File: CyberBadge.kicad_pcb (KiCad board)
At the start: 2 copper layers, 87.5 x 41 mm, 382 parts, among them J1 USB_C_Receptacle_USB2.0, J2 BAT_CONN, Q1 MMBT3904, Q2 MMBT3904, SW1 B_RST, SW2 B1/BOOT, U1 USBLC6-2SC6, U2 CP2102N-A01-GQFN28, U3 ESP32-WROOM-32, U4 SPX3819M5-L-3-3, U5 BQ24073RGT

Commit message: i forgor
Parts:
- removed REF**: SW_SPDT_PCM12, Button_Switch_SMD:SW_SPDT_PCM12
- added C180: 100n, Capacitor_SMD:C_0201_0603Metric, F.Cu at (143.5, 119.5)
- added Q3: FS8205A, Package_SO:TSSOP-8_4.4x3mm_P0.65mm, F.Cu at (151.2, 111.2)
- added R19: 200, Resistor_SMD:R_0201_0603Metric, F.Cu at (145.9, 119.5)
- added R20: 1k, Resistor_SMD:R_0201_0603Metric, F.Cu at (148.4, 119.5)
- added R21: 10k, Resistor_SMD:R_0201_0603Metric, F.Cu at (152.2, 119.4)
- added U6: DW01x, Package_TO_SOT_SMD:SOT-23-6, F.Cu at (153.6, 116.3)
- moved C10 0.80 mm to (149.9, 99.0)
- moved C7 0.80 mm to (146.4, 102.5)
- moved C8 0.80 mm to (143.9, 100.5)
- moved R16 0.80 mm to (144.9, 100.5)
- moved R17 0.80 mm to (148.4, 102.5)
- moved R18 0.80 mm to (149.9, 100.0)
- moved U5 0.80 mm to (147.4, 100.0)
- moved U1 0.32 mm to (152.3, 105.1)

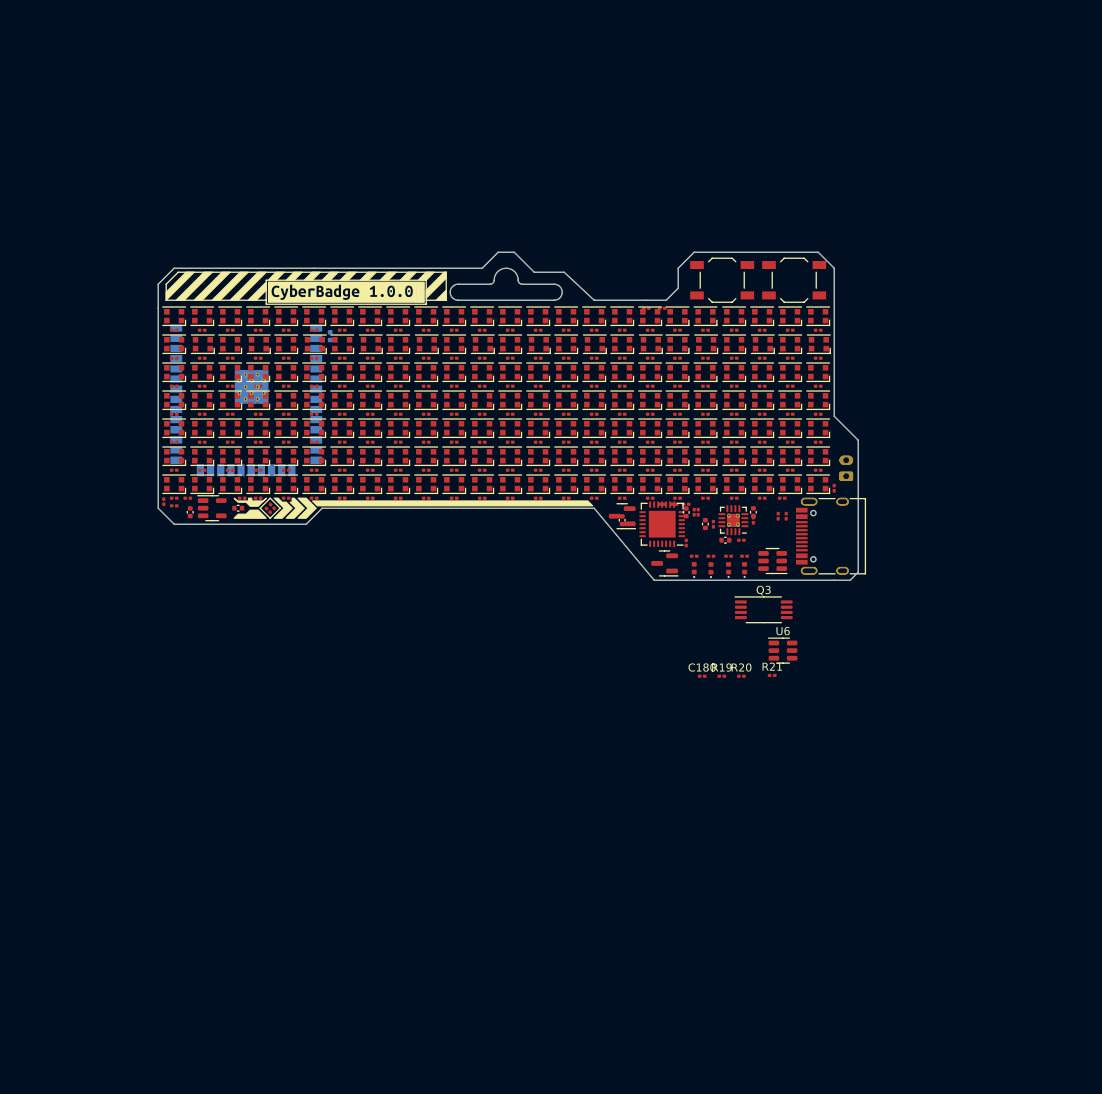
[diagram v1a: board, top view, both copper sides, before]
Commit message: change pixel count
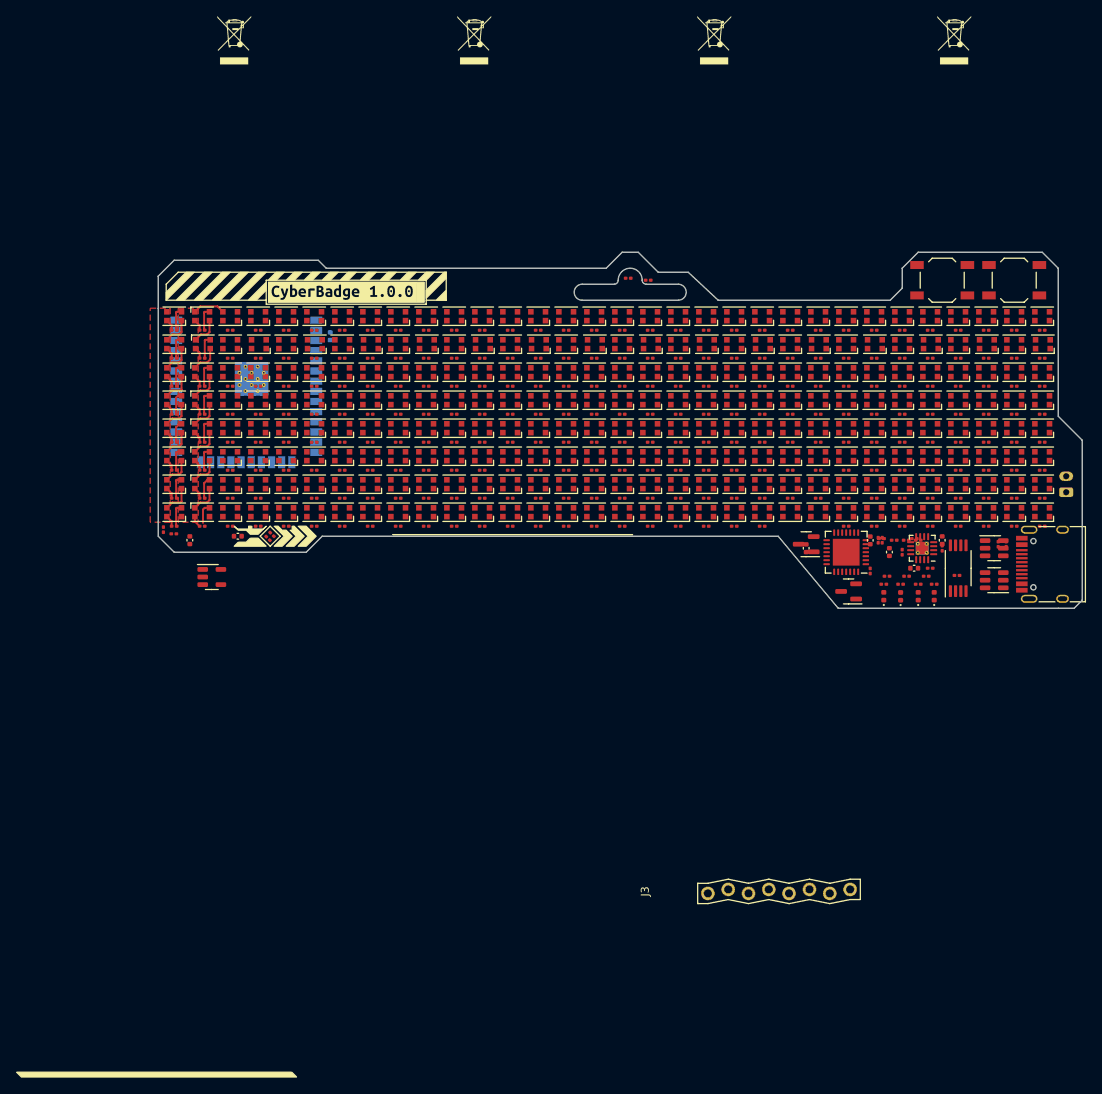
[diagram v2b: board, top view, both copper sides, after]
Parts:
- added C181: 100n, Capacitor_SMD:C_0201_0603Metric, F.Cu at (77.5, 97.2)
- added C182: 100n, Capacitor_SMD:C_0201_0603Metric, F.Cu at (81.0, 97.2)
- added C183: 100n, Capacitor_SMD:C_0201_0603Metric, F.Cu at (84.5, 97.2)
- added C184: 100n, Capacitor_SMD:C_0201_0603Metric, F.Cu at (88.0, 97.2)
- added C185: 100n, Capacitor_SMD:C_0201_0603Metric, F.Cu at (91.5, 97.2)
- added C186: 100n, Capacitor_SMD:C_0201_0603Metric, F.Cu at (95.0, 97.2)
- added C187: 100n, Capacitor_SMD:C_0201_0603Metric, F.Cu at (98.5, 97.2)
- added C188: 100n, Capacitor_SMD:C_0201_0603Metric, F.Cu at (102.0, 97.2)
- added C189: 100n, Capacitor_SMD:C_0201_0603Metric, F.Cu at (105.5, 97.2)
- added C190: 100n, Capacitor_SMD:C_0201_0603Metric, F.Cu at (109.0, 97.2)
- added C191: 100n, Capacitor_SMD:C_0201_0603Metric, F.Cu at (112.5, 97.2)
- added C192: 100n, Capacitor_SMD:C_0201_0603Metric, F.Cu at (116.0, 97.2)
- added C193: 100n, Capacitor_SMD:C_0201_0603Metric, F.Cu at (119.5, 97.2)
- added C194: 100n, Capacitor_SMD:C_0201_0603Metric, F.Cu at (123.0, 97.2)
- added C195: 100n, Capacitor_SMD:C_0201_0603Metric, F.Cu at (126.5, 97.2)
- added C196: 100n, Capacitor_SMD:C_0201_0603Metric, F.Cu at (130.0, 97.2)
- added C197: 100n, Capacitor_SMD:C_0201_0603Metric, F.Cu at (133.5, 97.2)
- added C198: 100n, Capacitor_SMD:C_0201_0603Metric, F.Cu at (137.0, 97.2)
- added C199: 100n, Capacitor_SMD:C_0201_0603Metric, F.Cu at (140.5, 97.2)
- added C200: 100n, Capacitor_SMD:C_0201_0603Metric, F.Cu at (144.0, 97.2)
- added C201: 100n, Capacitor_SMD:C_0201_0603Metric, F.Cu at (147.5, 97.2)
- added C202: 100n, Capacitor_SMD:C_0201_0603Metric, F.Cu at (151.0, 97.2)
- added C203: 100n, Capacitor_SMD:C_0201_0603Metric, F.Cu at (154.5, 97.2)
- added C204: 100n, Capacitor_SMD:C_0201_0603Metric, F.Cu at (158.0, 97.2)
- added C205: 100n, Capacitor_SMD:C_0201_0603Metric, F.Cu at (161.5, 76.2)
- added C206: 100n, Capacitor_SMD:C_0201_0603Metric, F.Cu at (165.0, 76.2)
- added C207: 100n, Capacitor_SMD:C_0201_0603Metric, F.Cu at (161.5, 79.8)
- added C208: 100n, Capacitor_SMD:C_0201_0603Metric, F.Cu at (165.0, 79.8)
- added C209: 100n, Capacitor_SMD:C_0201_0603Metric, F.Cu at (161.5, 83.2)
- added C210: 100n, Capacitor_SMD:C_0201_0603Metric, F.Cu at (165.0, 83.2)
- added C211: 100n, Capacitor_SMD:C_0201_0603Metric, F.Cu at (161.5, 86.8)
- added C212: 100n, Capacitor_SMD:C_0201_0603Metric, F.Cu at (165.0, 86.8)
- added C213: 100n, Capacitor_SMD:C_0201_0603Metric, F.Cu at (161.5, 90.2)
- added C214: 100n, Capacitor_SMD:C_0201_0603Metric, F.Cu at (165.0, 90.2)
- added C215: 100n, Capacitor_SMD:C_0201_0603Metric, F.Cu at (161.5, 93.8)
- added C216: 100n, Capacitor_SMD:C_0201_0603Metric, F.Cu at (165.0, 93.8)
- added C217: 100n, Capacitor_SMD:C_0201_0603Metric, F.Cu at (161.5, 97.2)
- added C218: 100n, Capacitor_SMD:C_0201_0603Metric, F.Cu at (165.0, 97.2)
- added C219: 100n, Capacitor_SMD:C_0201_0603Metric, F.Cu at (161.5, 100.8)
- added C220: 100n, Capacitor_SMD:C_0201_0603Metric, F.Cu at (165.0, 100.8)
- added C221: 100n, Capacitor_SMD:C_0201_0603Metric, F.Cu at (168.5, 76.2)
- added C222: 100n, Capacitor_SMD:C_0201_0603Metric, F.Cu at (172.0, 76.2)
- added C223: 100n, Capacitor_SMD:C_0201_0603Metric, F.Cu at (168.5, 79.8)
- added C224: 100n, Capacitor_SMD:C_0201_0603Metric, F.Cu at (172.0, 79.8)
- added C225: 100n, Capacitor_SMD:C_0201_0603Metric, F.Cu at (168.5, 83.2)
- added C226: 100n, Capacitor_SMD:C_0201_0603Metric, F.Cu at (172.0, 83.2)
- added C227: 100n, Capacitor_SMD:C_0201_0603Metric, F.Cu at (168.5, 86.8)
- added C228: 100n, Capacitor_SMD:C_0201_0603Metric, F.Cu at (172.0, 86.8)
- added C229: 100n, Capacitor_SMD:C_0201_0603Metric, F.Cu at (168.5, 90.2)
- added C230: 100n, Capacitor_SMD:C_0201_0603Metric, F.Cu at (172.0, 90.2)
- added C231: 100n, Capacitor_SMD:C_0201_0603Metric, F.Cu at (168.5, 93.8)
- added C232: 100n, Capacitor_SMD:C_0201_0603Metric, F.Cu at (172.0, 93.8)
- added C233: 100n, Capacitor_SMD:C_0201_0603Metric, F.Cu at (168.5, 97.2)
- added C234: 100n, Capacitor_SMD:C_0201_0603Metric, F.Cu at (172.0, 97.2)
- added C235: 100n, Capacitor_SMD:C_0201_0603Metric, F.Cu at (168.5, 100.8)
- added C236: 100n, Capacitor_SMD:C_0201_0603Metric, F.Cu at (172.0, 100.8)
- added C237: 100n, Capacitor_SMD:C_0201_0603Metric, F.Cu at (175.5, 76.2)
- added C238: 100n, Capacitor_SMD:C_0201_0603Metric, F.Cu at (179.0, 76.2)
- added C239: 100n, Capacitor_SMD:C_0201_0603Metric, F.Cu at (175.5, 79.8)
- added C240: 100n, Capacitor_SMD:C_0201_0603Metric, F.Cu at (179.0, 79.8)
- added C241: 100n, Capacitor_SMD:C_0201_0603Metric, F.Cu at (175.5, 83.2)
- added C242: 100n, Capacitor_SMD:C_0201_0603Metric, F.Cu at (179.0, 83.2)
- added C243: 100n, Capacitor_SMD:C_0201_0603Metric, F.Cu at (175.5, 86.8)
- added C244: 100n, Capacitor_SMD:C_0201_0603Metric, F.Cu at (179.0, 86.8)
- added C245: 100n, Capacitor_SMD:C_0201_0603Metric, F.Cu at (175.5, 90.2)
- added C246: 100n, Capacitor_SMD:C_0201_0603Metric, F.Cu at (179.0, 90.2)
- added C247: 100n, Capacitor_SMD:C_0201_0603Metric, F.Cu at (175.5, 93.8)
- added C248: 100n, Capacitor_SMD:C_0201_0603Metric, F.Cu at (179.0, 93.8)
- added C249: 100n, Capacitor_SMD:C_0201_0603Metric, F.Cu at (175.5, 97.2)
- added C250: 100n, Capacitor_SMD:C_0201_0603Metric, F.Cu at (179.0, 97.2)
- added C251: 100n, Capacitor_SMD:C_0201_0603Metric, F.Cu at (175.5, 100.8)
- added C252: 100n, Capacitor_SMD:C_0201_0603Metric, F.Cu at (179.0, 100.8)
- added C253: 100n, Capacitor_SMD:C_0201_0603Metric, F.Cu at (182.5, 76.2)
- added C254: 100n, Capacitor_SMD:C_0201_0603Metric, F.Cu at (186.0, 76.2)
- added C255: 100n, Capacitor_SMD:C_0201_0603Metric, F.Cu at (182.5, 79.8)
- added C256: 100n, Capacitor_SMD:C_0201_0603Metric, F.Cu at (186.0, 79.8)
- added C257: 100n, Capacitor_SMD:C_0201_0603Metric, F.Cu at (182.5, 83.2)
- added C258: 100n, Capacitor_SMD:C_0201_0603Metric, F.Cu at (186.0, 83.2)
- added C259: 100n, Capacitor_SMD:C_0201_0603Metric, F.Cu at (182.5, 86.8)
- added C260: 100n, Capacitor_SMD:C_0201_0603Metric, F.Cu at (186.0, 86.8)
- added C261: 100n, Capacitor_SMD:C_0201_0603Metric, F.Cu at (182.5, 90.2)
- added C262: 100n, Capacitor_SMD:C_0201_0603Metric, F.Cu at (186.0, 90.2)
- added C263: 100n, Capacitor_SMD:C_0201_0603Metric, F.Cu at (182.5, 93.8)
- added C264: 100n, Capacitor_SMD:C_0201_0603Metric, F.Cu at (186.0, 93.8)
- added C265: 100n, Capacitor_SMD:C_0201_0603Metric, F.Cu at (182.5, 97.2)
- added C266: 100n, Capacitor_SMD:C_0201_0603Metric, F.Cu at (186.0, 97.2)
- added C267: 100n, Capacitor_SMD:C_0201_0603Metric, F.Cu at (182.5, 100.8)
- added C268: 100n, Capacitor_SMD:C_0201_0603Metric, F.Cu at (186.0, 100.8)
- added D173: WS2812B, Critbit_lib:LED_WS2812B-2020_pinsRenumbered, F.Cu at (77.5, 95.5)
- added D174: WS2812B, Critbit_lib:LED_WS2812B-2020_pinsRenumbered, F.Cu at (81.0, 95.5)
- added D175: WS2812B, Critbit_lib:LED_WS2812B-2020_pinsRenumbered, F.Cu at (84.5, 95.5)
- added D176: WS2812B, Critbit_lib:LED_WS2812B-2020_pinsRenumbered, F.Cu at (88.0, 95.5)
- added D177: WS2812B, Critbit_lib:LED_WS2812B-2020_pinsRenumbered, F.Cu at (91.5, 95.5)
- added D178: WS2812B, Critbit_lib:LED_WS2812B-2020_pinsRenumbered, F.Cu at (95.0, 95.5)
- added D179: WS2812B, Critbit_lib:LED_WS2812B-2020_pinsRenumbered, F.Cu at (98.5, 95.5)
- added D180: WS2812B, Critbit_lib:LED_WS2812B-2020_pinsRenumbered, F.Cu at (102.0, 95.5)
- added D181: WS2812B, Critbit_lib:LED_WS2812B-2020_pinsRenumbered, F.Cu at (105.5, 95.5)
- added D182: WS2812B, Critbit_lib:LED_WS2812B-2020_pinsRenumbered, F.Cu at (109.0, 95.5)
- added D183: WS2812B, Critbit_lib:LED_WS2812B-2020_pinsRenumbered, F.Cu at (112.5, 95.5)
- added D184: WS2812B, Critbit_lib:LED_WS2812B-2020_pinsRenumbered, F.Cu at (116.0, 95.5)
- added D185: WS2812B, Critbit_lib:LED_WS2812B-2020_pinsRenumbered, F.Cu at (119.5, 95.5)
- added D186: WS2812B, Critbit_lib:LED_WS2812B-2020_pinsRenumbered, F.Cu at (123.0, 95.5)
- added D187: WS2812B, Critbit_lib:LED_WS2812B-2020_pinsRenumbered, F.Cu at (126.5, 95.5)
- added D188: WS2812B, Critbit_lib:LED_WS2812B-2020_pinsRenumbered, F.Cu at (130.0, 95.5)
- added D189: WS2812B, Critbit_lib:LED_WS2812B-2020_pinsRenumbered, F.Cu at (133.5, 95.5)
- added D190: WS2812B, Critbit_lib:LED_WS2812B-2020_pinsRenumbered, F.Cu at (137.0, 95.5)
- added D191: WS2812B, Critbit_lib:LED_WS2812B-2020_pinsRenumbered, F.Cu at (140.5, 95.5)
- added D192: WS2812B, Critbit_lib:LED_WS2812B-2020_pinsRenumbered, F.Cu at (144.0, 95.5)
- added D193: WS2812B, Critbit_lib:LED_WS2812B-2020_pinsRenumbered, F.Cu at (147.5, 95.5)
- added D194: WS2812B, Critbit_lib:LED_WS2812B-2020_pinsRenumbered, F.Cu at (151.0, 95.5)
- added D195: WS2812B, Critbit_lib:LED_WS2812B-2020_pinsRenumbered, F.Cu at (154.5, 95.5)
- added D196: WS2812B, Critbit_lib:LED_WS2812B-2020_pinsRenumbered, F.Cu at (158.0, 95.5)
- added D197: WS2812B, Critbit_lib:LED_WS2812B-2020_pinsRenumbered, F.Cu at (161.5, 74.5)
- added D198: WS2812B, Critbit_lib:LED_WS2812B-2020_pinsRenumbered, F.Cu at (165.0, 74.5)
- added D199: WS2812B, Critbit_lib:LED_WS2812B-2020_pinsRenumbered, F.Cu at (161.5, 78.0)
- added D200: WS2812B, Critbit_lib:LED_WS2812B-2020_pinsRenumbered, F.Cu at (165.1, 78.0)
- added D201: WS2812B, Critbit_lib:LED_WS2812B-2020_pinsRenumbered, F.Cu at (161.5, 81.5)
- added D202: WS2812B, Critbit_lib:LED_WS2812B-2020_pinsRenumbered, F.Cu at (165.0, 81.5)
- added D203: WS2812B, Critbit_lib:LED_WS2812B-2020_pinsRenumbered, F.Cu at (161.5, 85.0)
- added D204: WS2812B, Critbit_lib:LED_WS2812B-2020_pinsRenumbered, F.Cu at (165.0, 85.0)
- added D205: WS2812B, Critbit_lib:LED_WS2812B-2020_pinsRenumbered, F.Cu at (161.5, 88.5)
- added D206: WS2812B, Critbit_lib:LED_WS2812B-2020_pinsRenumbered, F.Cu at (165.0, 88.5)
- added D207: WS2812B, Critbit_lib:LED_WS2812B-2020_pinsRenumbered, F.Cu at (161.5, 92.0)
- added D208: WS2812B, Critbit_lib:LED_WS2812B-2020_pinsRenumbered, F.Cu at (165.0, 92.0)
- added D209: WS2812B, Critbit_lib:LED_WS2812B-2020_pinsRenumbered, F.Cu at (161.5, 95.5)
- added D210: WS2812B, Critbit_lib:LED_WS2812B-2020_pinsRenumbered, F.Cu at (165.0, 95.5)
- added D211: WS2812B, Critbit_lib:LED_WS2812B-2020_pinsRenumbered, F.Cu at (161.5, 99.0)
- added D212: WS2812B, Critbit_lib:LED_WS2812B-2020_pinsRenumbered, F.Cu at (165.0, 99.0)
- added D213: WS2812B, Critbit_lib:LED_WS2812B-2020_pinsRenumbered, F.Cu at (168.5, 74.5)
- added D214: WS2812B, Critbit_lib:LED_WS2812B-2020_pinsRenumbered, F.Cu at (172.0, 74.5)
- added D215: WS2812B, Critbit_lib:LED_WS2812B-2020_pinsRenumbered, F.Cu at (168.5, 78.0)
- added D216: WS2812B, Critbit_lib:LED_WS2812B-2020_pinsRenumbered, F.Cu at (172.1, 78.0)
- added D217: WS2812B, Critbit_lib:LED_WS2812B-2020_pinsRenumbered, F.Cu at (168.5, 81.5)
- added D218: WS2812B, Critbit_lib:LED_WS2812B-2020_pinsRenumbered, F.Cu at (172.0, 81.5)
- added D219: WS2812B, Critbit_lib:LED_WS2812B-2020_pinsRenumbered, F.Cu at (168.5, 85.0)
- added D220: WS2812B, Critbit_lib:LED_WS2812B-2020_pinsRenumbered, F.Cu at (172.0, 85.0)
- added D221: WS2812B, Critbit_lib:LED_WS2812B-2020_pinsRenumbered, F.Cu at (168.5, 88.5)
- added D222: WS2812B, Critbit_lib:LED_WS2812B-2020_pinsRenumbered, F.Cu at (172.0, 88.5)
- added D223: WS2812B, Critbit_lib:LED_WS2812B-2020_pinsRenumbered, F.Cu at (168.5, 92.0)
- added D224: WS2812B, Critbit_lib:LED_WS2812B-2020_pinsRenumbered, F.Cu at (172.0, 92.0)
- added D225: WS2812B, Critbit_lib:LED_WS2812B-2020_pinsRenumbered, F.Cu at (168.5, 95.5)
- added D226: WS2812B, Critbit_lib:LED_WS2812B-2020_pinsRenumbered, F.Cu at (172.0, 95.5)
- added D227: WS2812B, Critbit_lib:LED_WS2812B-2020_pinsRenumbered, F.Cu at (168.5, 99.0)
- added D228: WS2812B, Critbit_lib:LED_WS2812B-2020_pinsRenumbered, F.Cu at (172.0, 99.0)
- added D229: WS2812B, Critbit_lib:LED_WS2812B-2020_pinsRenumbered, F.Cu at (175.5, 74.5)
- added D230: WS2812B, Critbit_lib:LED_WS2812B-2020_pinsRenumbered, F.Cu at (179.0, 74.5)
- added D231: WS2812B, Critbit_lib:LED_WS2812B-2020_pinsRenumbered, F.Cu at (175.5, 78.0)
- added D232: WS2812B, Critbit_lib:LED_WS2812B-2020_pinsRenumbered, F.Cu at (179.1, 78.0)
- added D233: WS2812B, Critbit_lib:LED_WS2812B-2020_pinsRenumbered, F.Cu at (175.5, 81.5)
- added D234: WS2812B, Critbit_lib:LED_WS2812B-2020_pinsRenumbered, F.Cu at (179.0, 81.5)
- added D235: WS2812B, Critbit_lib:LED_WS2812B-2020_pinsRenumbered, F.Cu at (175.5, 85.0)
- added D236: WS2812B, Critbit_lib:LED_WS2812B-2020_pinsRenumbered, F.Cu at (179.0, 85.0)
- added D237: WS2812B, Critbit_lib:LED_WS2812B-2020_pinsRenumbered, F.Cu at (175.5, 88.5)
- added D238: WS2812B, Critbit_lib:LED_WS2812B-2020_pinsRenumbered, F.Cu at (179.0, 88.5)
- added D239: WS2812B, Critbit_lib:LED_WS2812B-2020_pinsRenumbered, F.Cu at (175.5, 92.0)
- added D240: WS2812B, Critbit_lib:LED_WS2812B-2020_pinsRenumbered, F.Cu at (179.0, 92.0)
- added D241: WS2812B, Critbit_lib:LED_WS2812B-2020_pinsRenumbered, F.Cu at (175.5, 95.5)
- added D242: WS2812B, Critbit_lib:LED_WS2812B-2020_pinsRenumbered, F.Cu at (179.0, 95.5)
- added D243: WS2812B, Critbit_lib:LED_WS2812B-2020_pinsRenumbered, F.Cu at (175.5, 99.0)
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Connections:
- C100 pad 1: +4V -> /PWR_LEDS
- C101 pad 1: +4V -> /PWR_LEDS
- C102 pad 1: +4V -> /PWR_LEDS
- C103 pad 1: +4V -> /PWR_LEDS
- C104 pad 1: +4V -> /PWR_LEDS
- C105 pad 1: +4V -> /PWR_LEDS
- C106 pad 1: +4V -> /PWR_LEDS
- C107 pad 1: +4V -> /PWR_LEDS
- C108 pad 1: +4V -> /PWR_LEDS
- C109 pad 1: +4V -> /PWR_LEDS
- C11 pad 1: +4V -> /PWR_LEDS
- C110 pad 1: +4V -> /PWR_LEDS
- C111 pad 1: +4V -> /PWR_LEDS
- C112 pad 1: +4V -> /PWR_LEDS
- C113 pad 1: +4V -> /PWR_LEDS
- C114 pad 1: +4V -> /PWR_LEDS
- C115 pad 1: +4V -> /PWR_LEDS
- C116 pad 1: +4V -> /PWR_LEDS
- C117 pad 1: +4V -> /PWR_LEDS
- C118 pad 1: +4V -> /PWR_LEDS
- C119 pad 1: +4V -> /PWR_LEDS
- C12 pad 1: +4V -> /PWR_LEDS
- C120 pad 1: +4V -> /PWR_LEDS
- C121 pad 1: +4V -> /PWR_LEDS
- C122 pad 1: +4V -> /PWR_LEDS
- C123 pad 1: +4V -> /PWR_LEDS
- C124 pad 1: +4V -> /PWR_LEDS
- C125 pad 1: +4V -> /PWR_LEDS
- C126 pad 1: +4V -> /PWR_LEDS
- C127 pad 1: +4V -> /PWR_LEDS
- C128 pad 1: +4V -> /PWR_LEDS
- C129 pad 1: +4V -> /PWR_LEDS
- C13 pad 1: +4V -> /PWR_LEDS
- C130 pad 1: +4V -> /PWR_LEDS
- C131 pad 1: +4V -> /PWR_LEDS
- C132 pad 1: +4V -> /PWR_LEDS
- C133 pad 1: +4V -> /PWR_LEDS
- C134 pad 1: +4V -> /PWR_LEDS
- C135 pad 1: +4V -> /PWR_LEDS
- C136 pad 1: +4V -> /PWR_LEDS
- C137 pad 1: +4V -> /PWR_LEDS
- C138 pad 1: +4V -> /PWR_LEDS
- C139 pad 1: +4V -> /PWR_LEDS
- C14 pad 1: +4V -> /PWR_LEDS
- C140 pad 1: +4V -> /PWR_LEDS
- C141 pad 1: +4V -> /PWR_LEDS
- C142 pad 1: +4V -> /PWR_LEDS
- C143 pad 1: +4V -> /PWR_LEDS
- C144 pad 1: +4V -> /PWR_LEDS
- C145 pad 1: +4V -> /PWR_LEDS
- C146 pad 1: +4V -> /PWR_LEDS
- C147 pad 1: +4V -> /PWR_LEDS
- C148 pad 1: +4V -> /PWR_LEDS
- C149 pad 1: +4V -> /PWR_LEDS
- C15 pad 1: +4V -> /PWR_LEDS
- C150 pad 1: +4V -> /PWR_LEDS
- C151 pad 1: +4V -> /PWR_LEDS
- C152 pad 1: +4V -> /PWR_LEDS
- C153 pad 1: +4V -> /PWR_LEDS
- C154 pad 1: +4V -> /PWR_LEDS
- C155 pad 1: +4V -> /PWR_LEDS
- C156 pad 1: +4V -> /PWR_LEDS
- C157 pad 1: +4V -> /PWR_LEDS
- C158 pad 1: +4V -> /PWR_LEDS
- C159 pad 1: +4V -> /PWR_LEDS
- C16 pad 1: +4V -> /PWR_LEDS
- C160 pad 1: +4V -> /PWR_LEDS
- C161 pad 1: +4V -> /PWR_LEDS
- C162 pad 1: +4V -> /PWR_LEDS
- C163 pad 1: +4V -> /PWR_LEDS
- C164 pad 1: +4V -> /PWR_LEDS
- C165 pad 1: +4V -> /PWR_LEDS
- C166 pad 1: +4V -> /PWR_LEDS
- C167 pad 1: +4V -> /PWR_LEDS
- C168 pad 1: +4V -> /PWR_LEDS
- C169 pad 1: +4V -> /PWR_LEDS
- C17 pad 1: +4V -> /PWR_LEDS
- C170 pad 1: +4V -> /PWR_LEDS
- C171 pad 1: +4V -> /PWR_LEDS
- C172 pad 1: +4V -> /PWR_LEDS
- C173 pad 1: +4V -> /PWR_LEDS
- C174 pad 1: +4V -> /PWR_LEDS
- C175 pad 1: +4V -> /PWR_LEDS
- C176 pad 1: +4V -> /PWR_LEDS
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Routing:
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- added copper zone on F.Cu, net +4V
- added copper zone on F.Cu, net GND
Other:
- board size 87.5 x 41 mm -> 115.5 x 44.5 mm

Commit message: commit before replicatelayout
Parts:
- removed C1, C4: 100n, Capacitor_SMD:C_0201_0603Metric
- removed C2, C3: 4.7u, Capacitor_SMD:C_0402_1005Metric
- removed D2: LED, LED_SMD:LED_0402_1005Metric
- removed R10, R11, R3: 2k, Resistor_SMD:R_0201_0603Metric
- removed R13, R6: 10k, Resistor_SMD:R_0201_0603Metric
- removed U1: USBLC6-2SC6, Package_TO_SOT_SMD:SOT-23-6
- removed U2: CP2102N-A01-GQFN28, Package_DFN_QFN:QFN-28-1EP_5x5mm_P0.5mm_EP3.35x3.35mm
- added F1: 3A/slowblow, Fuse:Fuse_0603_1608Metric_Pad1.05x0.95mm_HandSolder, F.Cu at (111.0, 106.2)
- added H1: SCRHOLE, MountingHole:MountingHole_3.2mm_M3, F.Cu at (79.0, 71.0)
- added H2: SCRHOLE, MountingHole:MountingHole_3.2mm_M3, F.Cu at (184.5, 70.0)
- added H3: SCRHOLE, MountingHole:MountingHole_3.2mm_M3, F.Cu at (79.0, 104.5)
- added H4: SCRHOLE, MountingHole:MountingHole_3.2mm_M3, F.Cu at (184.5, 104.5)
- added Q4: AO3401A, Package_TO_SOT_SMD:SOT-23, F.Cu at (121.1, 103.5)
- added SW3: SW_SPDT, Button_Switch_SMD:SW_SPDT_PCM12, F.Cu at (154.5, 70.1)
- added SW4: RST, Button_Switch_SMD:SW_SPST_FSMSM, B.Cu at (103.8, 84.5)
- J3: moved to B.Cu
- SW1: value B_RST -> B2
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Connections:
- C100 pad 1: /PWR_LEDS -> +4V
- C101 pad 1: /PWR_LEDS -> +4V
- C102 pad 1: /PWR_LEDS -> +4V
- C103 pad 1: /PWR_LEDS -> +4V
- C104 pad 1: /PWR_LEDS -> +4V
- C105 pad 1: /PWR_LEDS -> +4V
- C106 pad 1: /PWR_LEDS -> +4V
- C107 pad 1: /PWR_LEDS -> +4V
- C108 pad 1: /PWR_LEDS -> +4V
- C109 pad 1: /PWR_LEDS -> +4V
- C11 pad 1: /PWR_LEDS -> +4V
- C110 pad 1: /PWR_LEDS -> +4V
- C111 pad 1: /PWR_LEDS -> +4V
- C112 pad 1: /PWR_LEDS -> +4V
- C113 pad 1: /PWR_LEDS -> +4V
- C114 pad 1: /PWR_LEDS -> +4V
- C115 pad 1: /PWR_LEDS -> +4V
- C116 pad 1: /PWR_LEDS -> +4V
- C117 pad 1: /PWR_LEDS -> +4V
- C118 pad 1: /PWR_LEDS -> +4V
- C119 pad 1: /PWR_LEDS -> +4V
- C12 pad 1: /PWR_LEDS -> +4V
- C120 pad 1: /PWR_LEDS -> +4V
- C121 pad 1: /PWR_LEDS -> +4V
- C122 pad 1: /PWR_LEDS -> +4V
- C123 pad 1: /PWR_LEDS -> +4V
- C124 pad 1: /PWR_LEDS -> +4V
- C125 pad 1: /PWR_LEDS -> +4V
- C126 pad 1: /PWR_LEDS -> +4V
- C127 pad 1: /PWR_LEDS -> +4V
- C128 pad 1: /PWR_LEDS -> +4V
- C129 pad 1: /PWR_LEDS -> +4V
- C13 pad 1: /PWR_LEDS -> +4V
- C130 pad 1: /PWR_LEDS -> +4V
- C131 pad 1: /PWR_LEDS -> +4V
- C132 pad 1: /PWR_LEDS -> +4V
- C133 pad 1: /PWR_LEDS -> +4V
- C134 pad 1: /PWR_LEDS -> +4V
- C135 pad 1: /PWR_LEDS -> +4V
- C136 pad 1: /PWR_LEDS -> +4V
- C137 pad 1: /PWR_LEDS -> +4V
- C138 pad 1: /PWR_LEDS -> +4V
- C139 pad 1: /PWR_LEDS -> +4V
- C14 pad 1: /PWR_LEDS -> +4V
- C140 pad 1: /PWR_LEDS -> +4V
- C141 pad 1: /PWR_LEDS -> +4V
- C142 pad 1: /PWR_LEDS -> +4V
- C143 pad 1: /PWR_LEDS -> +4V
- C144 pad 1: /PWR_LEDS -> +4V
- C145 pad 1: /PWR_LEDS -> +4V
- C146 pad 1: /PWR_LEDS -> +4V
- C147 pad 1: /PWR_LEDS -> +4V
- C148 pad 1: /PWR_LEDS -> +4V
- C149 pad 1: /PWR_LEDS -> +4V
- C15 pad 1: /PWR_LEDS -> +4V
- C150 pad 1: /PWR_LEDS -> +4V
- C151 pad 1: /PWR_LEDS -> +4V
- C152 pad 1: /PWR_LEDS -> +4V
- C153 pad 1: /PWR_LEDS -> +4V
- C154 pad 1: /PWR_LEDS -> +4V
- C155 pad 1: /PWR_LEDS -> +4V
- C156 pad 1: /PWR_LEDS -> +4V
- C157 pad 1: /PWR_LEDS -> +4V
- C158 pad 1: /PWR_LEDS -> +4V
- C159 pad 1: /PWR_LEDS -> +4V
- C16 pad 1: /PWR_LEDS -> +4V
- C160 pad 1: /PWR_LEDS -> +4V
- C161 pad 1: /PWR_LEDS -> +4V
- C162 pad 1: /PWR_LEDS -> +4V
- C163 pad 1: /PWR_LEDS -> +4V
- C164 pad 1: /PWR_LEDS -> +4V
- C165 pad 1: /PWR_LEDS -> +4V
- C166 pad 1: /PWR_LEDS -> +4V
- C167 pad 1: /PWR_LEDS -> +4V
- C168 pad 1: /PWR_LEDS -> +4V
- C169 pad 1: /PWR_LEDS -> +4V
- C17 pad 1: /PWR_LEDS -> +4V
- C170 pad 1: /PWR_LEDS -> +4V
- C171 pad 1: /PWR_LEDS -> +4V
- C172 pad 1: /PWR_LEDS -> +4V
- C173 pad 1: /PWR_LEDS -> +4V
- C174 pad 1: /PWR_LEDS -> +4V
- C175 pad 1: /PWR_LEDS -> +4V
- C176 pad 1: /PWR_LEDS -> +4V
- C177 pad 1: /PWR_LEDS -> +4V
- C178 pad 1: /PWR_LEDS -> +4V
- C179 pad 1: Net-(C179-Pad1) -> +3.3V
- C18 pad 1: /PWR_LEDS -> +4V
- C181 pad 1: /PWR_LEDS -> +4V
- C182 pad 1: /PWR_LEDS -> +4V
- C183 pad 1: /PWR_LEDS -> +4V
- C184 pad 1: /PWR_LEDS -> +4V
- C185 pad 1: /PWR_LEDS -> +4V
- C186 pad 1: /PWR_LEDS -> +4V
- C187 pad 1: /PWR_LEDS -> +4V
- C188 pad 1: /PWR_LEDS -> +4V
- C189 pad 1: /PWR_LEDS -> +4V
- C19 pad 1: /PWR_LEDS -> +4V
- C190 pad 1: /PWR_LEDS -> +4V
- C191 pad 1: /PWR_LEDS -> +4V
- C192 pad 1: /PWR_LEDS -> +4V
- C193 pad 1: /PWR_LEDS -> +4V
- C194 pad 1: /PWR_LEDS -> +4V
- C195 pad 1: /PWR_LEDS -> +4V
- C196 pad 1: /PWR_LEDS -> +4V
- C197 pad 1: /PWR_LEDS -> +4V
- C198 pad 1: /PWR_LEDS -> +4V
- C199 pad 1: /PWR_LEDS -> +4V
- C20 pad 1: /PWR_LEDS -> +4V
- C200 pad 1: /PWR_LEDS -> +4V
- C201 pad 1: /PWR_LEDS -> +4V
- C202 pad 1: /PWR_LEDS -> +4V
- C203 pad 1: /PWR_LEDS -> +4V
- C204 pad 1: /PWR_LEDS -> +4V
- C205 pad 1: /PWR_LEDS -> +4V
- C206 pad 1: /PWR_LEDS -> +4V
- C207 pad 1: /PWR_LEDS -> +4V
- C208 pad 1: /PWR_LEDS -> +4V
- C209 pad 1: /PWR_LEDS -> +4V
- C21 pad 1: /PWR_LEDS -> +4V
- C210 pad 1: /PWR_LEDS -> +4V
- C211 pad 1: /PWR_LEDS -> +4V
- C212 pad 1: /PWR_LEDS -> +4V
- C213 pad 1: /PWR_LEDS -> +4V
- C214 pad 1: /PWR_LEDS -> +4V
- C215 pad 1: /PWR_LEDS -> +4V
- C216 pad 1: /PWR_LEDS -> +4V
- C217 pad 1: /PWR_LEDS -> +4V
- C218 pad 1: /PWR_LEDS -> +4V
- C219 pad 1: /PWR_LEDS -> +4V
- C22 pad 1: /PWR_LEDS -> +4V
- C220 pad 1: /PWR_LEDS -> +4V
- C221 pad 1: /PWR_LEDS -> +4V
- C222 pad 1: /PWR_LEDS -> +4V
- C223 pad 1: /PWR_LEDS -> +4V
- C224 pad 1: /PWR_LEDS -> +4V
- C225 pad 1: /PWR_LEDS -> +4V
- C226 pad 1: /PWR_LEDS -> +4V
- C227 pad 1: /PWR_LEDS -> +4V
- C228 pad 1: /PWR_LEDS -> +4V
- C229 pad 1: /PWR_LEDS -> +4V
- C23 pad 1: /PWR_LEDS -> +4V
- C230 pad 1: /PWR_LEDS -> +4V
- C231 pad 1: /PWR_LEDS -> +4V
- C232 pad 1: /PWR_LEDS -> +4V
- C233 pad 1: /PWR_LEDS -> +4V
- C234 pad 1: /PWR_LEDS -> +4V
- C235 pad 1: /PWR_LEDS -> +4V
- C236 pad 1: /PWR_LEDS -> +4V
- C237 pad 1: /PWR_LEDS -> +4V
- C238 pad 1: /PWR_LEDS -> +4V
- C239 pad 1: /PWR_LEDS -> +4V
- C24 pad 1: /PWR_LEDS -> +4V
- C240 pad 1: /PWR_LEDS -> +4V
- C241 pad 1: /PWR_LEDS -> +4V
- C242 pad 1: /PWR_LEDS -> +4V
- C243 pad 1: /PWR_LEDS -> +4V
- C244 pad 1: /PWR_LEDS -> +4V
- C245 pad 1: /PWR_LEDS -> +4V
- C246 pad 1: /PWR_LEDS -> +4V
- C247 pad 1: /PWR_LEDS -> +4V
- C248 pad 1: /PWR_LEDS -> +4V
- C249 pad 1: /PWR_LEDS -> +4V
- C25 pad 1: /PWR_LEDS -> +4V
- C250 pad 1: /PWR_LEDS -> +4V
- C251 pad 1: /PWR_LEDS -> +4V
- C252 pad 1: /PWR_LEDS -> +4V
- C253 pad 1: /PWR_LEDS -> +4V
- C254 pad 1: /PWR_LEDS -> +4V
- C255 pad 1: /PWR_LEDS -> +4V
- C256 pad 1: /PWR_LEDS -> +4V
- C257 pad 1: /PWR_LEDS -> +4V
- C258 pad 1: /PWR_LEDS -> +4V
- C259 pad 1: /PWR_LEDS -> +4V
- C26 pad 1: /PWR_LEDS -> +4V
- C260 pad 1: /PWR_LEDS -> +4V
- C261 pad 1: /PWR_LEDS -> +4V
- C262 pad 1: /PWR_LEDS -> +4V
- C263 pad 1: /PWR_LEDS -> +4V
- C264 pad 1: /PWR_LEDS -> +4V
- C265 pad 1: /PWR_LEDS -> +4V
- C266 pad 1: /PWR_LEDS -> +4V
- C267 pad 1: /PWR_LEDS -> +4V
- C268 pad 1: /PWR_LEDS -> +4V
- C27 pad 1: /PWR_LEDS -> +4V
- C28 pad 1: /PWR_LEDS -> +4V
- C29 pad 1: /PWR_LEDS -> +4V
- C30 pad 1: /PWR_LEDS -> +4V
- C31 pad 1: /PWR_LEDS -> +4V
- C32 pad 1: /PWR_LEDS -> +4V
- C33 pad 1: /PWR_LEDS -> +4V
- C34 pad 1: /PWR_LEDS -> +4V
- C35 pad 1: /PWR_LEDS -> +4V
- C36 pad 1: /PWR_LEDS -> +4V
- C37 pad 1: /PWR_LEDS -> +4V
- C38 pad 1: /PWR_LEDS -> +4V
- C39 pad 1: /PWR_LEDS -> +4V
- C40 pad 1: /PWR_LEDS -> +4V
- C41 pad 1: /PWR_LEDS -> +4V
- C42 pad 1: /PWR_LEDS -> +4V
- C43 pad 1: /PWR_LEDS -> +4V
- C44 pad 1: /PWR_LEDS -> +4V
- C45 pad 1: /PWR_LEDS -> +4V
- C46 pad 1: /PWR_LEDS -> +4V
- C47 pad 1: /PWR_LEDS -> +4V
- C48 pad 1: /PWR_LEDS -> +4V
- C49 pad 1: /PWR_LEDS -> +4V
- C50 pad 1: /PWR_LEDS -> +4V
- C51 pad 1: /PWR_LEDS -> +4V
- C52 pad 1: /PWR_LEDS -> +4V
- C53 pad 1: /PWR_LEDS -> +4V
- C54 pad 1: /PWR_LEDS -> +4V
- C55 pad 1: /PWR_LEDS -> +4V
- C56 pad 1: /PWR_LEDS -> +4V
- C57 pad 1: /PWR_LEDS -> +4V
- C58 pad 1: /PWR_LEDS -> +4V
- C59 pad 1: /PWR_LEDS -> +4V
- C60 pad 1: /PWR_LEDS -> +4V
- C61 pad 1: /PWR_LEDS -> +4V
- C62 pad 1: /PWR_LEDS -> +4V
- C63 pad 1: /PWR_LEDS -> +4V
- C64 pad 1: /PWR_LEDS -> +4V
- C65 pad 1: /PWR_LEDS -> +4V
- C66 pad 1: /PWR_LEDS -> +4V
- C67 pad 1: /PWR_LEDS -> +4V
- C68 pad 1: /PWR_LEDS -> +4V
- C69 pad 1: /PWR_LEDS -> +4V
- C70 pad 1: /PWR_LEDS -> +4V
- C71 pad 1: /PWR_LEDS -> +4V
- C72 pad 1: /PWR_LEDS -> +4V
- C73 pad 1: /PWR_LEDS -> +4V
- C74 pad 1: /PWR_LEDS -> +4V
- C75 pad 1: /PWR_LEDS -> +4V
- C76 pad 1: /PWR_LEDS -> +4V
- C77 pad 1: /PWR_LEDS -> +4V
- C78 pad 1: /PWR_LEDS -> +4V
- C79 pad 1: /PWR_LEDS -> +4V
- C8 pad 1: +4V -> /LIPO_PRE_MOSFET
- C80 pad 1: /PWR_LEDS -> +4V
- C81 pad 1: /PWR_LEDS -> +4V
- C82 pad 1: /PWR_LEDS -> +4V
- C83 pad 1: /PWR_LEDS -> +4V
- C84 pad 1: /PWR_LEDS -> +4V
- C85 pad 1: /PWR_LEDS -> +4V
- C86 pad 1: /PWR_LEDS -> +4V
- C87 pad 1: /PWR_LEDS -> +4V
- C88 pad 1: /PWR_LEDS -> +4V
- C89 pad 1: /PWR_LEDS -> +4V
- C90 pad 1: /PWR_LEDS -> +4V
- C91 pad 1: /PWR_LEDS -> +4V
- C92 pad 1: /PWR_LEDS -> +4V
- C93 pad 1: /PWR_LEDS -> +4V
- C94 pad 1: /PWR_LEDS -> +4V
- C95 pad 1: /PWR_LEDS -> +4V
- C96 pad 1: /PWR_LEDS -> +4V
- C97 pad 1: /PWR_LEDS -> +4V
- C98 pad 1: /PWR_LEDS -> +4V
- C99 pad 1: /PWR_LEDS -> +4V
- D1 pad 2: Net-(D1-Pad2) -> +4V
- D10 pad 1: /PWR_LEDS -> +4V
- D100 pad 1: /PWR_LEDS -> +4V
- D101 pad 1: /PWR_LEDS -> +4V
- D102 pad 1: /PWR_LEDS -> +4V
- D103 pad 1: /PWR_LEDS -> +4V
- D104 pad 1: /PWR_LEDS -> +4V
- D105 pad 1: /PWR_LEDS -> +4V
- D106 pad 1: /PWR_LEDS -> +4V
- D107 pad 1: /PWR_LEDS -> +4V
- D108 pad 1: /PWR_LEDS -> +4V
- D109 pad 1: /PWR_LEDS -> +4V
- D11 pad 1: /PWR_LEDS -> +4V
- D110 pad 1: /PWR_LEDS -> +4V
- D111 pad 1: /PWR_LEDS -> +4V
- D112 pad 1: /PWR_LEDS -> +4V
- D113 pad 1: /PWR_LEDS -> +4V
- D114 pad 1: /PWR_LEDS -> +4V
- D115 pad 1: /PWR_LEDS -> +4V
- D116 pad 1: /PWR_LEDS -> +4V
- D117 pad 1: /PWR_LEDS -> +4V
- D118 pad 1: /PWR_LEDS -> +4V
- D119 pad 1: /PWR_LEDS -> +4V
- D12 pad 1: /PWR_LEDS -> +4V
- D120 pad 1: /PWR_LEDS -> +4V
- D121 pad 1: /PWR_LEDS -> +4V
- D122 pad 1: /PWR_LEDS -> +4V
- D123 pad 1: /PWR_LEDS -> +4V
- D124 pad 1: /PWR_LEDS -> +4V
- D125 pad 1: /PWR_LEDS -> +4V
- D126 pad 1: /PWR_LEDS -> +4V
- D127 pad 1: /PWR_LEDS -> +4V
- D128 pad 1: /PWR_LEDS -> +4V
- D129 pad 1: /PWR_LEDS -> +4V
- D13 pad 1: /PWR_LEDS -> +4V
- D130 pad 1: /PWR_LEDS -> +4V
- D131 pad 1: /PWR_LEDS -> +4V
- D132 pad 1: /PWR_LEDS -> +4V
- D133 pad 1: /PWR_LEDS -> +4V
- D134 pad 1: /PWR_LEDS -> +4V
- D135 pad 1: /PWR_LEDS -> +4V
- D136 pad 1: /PWR_LEDS -> +4V
- D137 pad 1: /PWR_LEDS -> +4V
- D138 pad 1: /PWR_LEDS -> +4V
- D139 pad 1: /PWR_LEDS -> +4V
- D14 pad 1: /PWR_LEDS -> +4V
- D140 pad 1: /PWR_LEDS -> +4V
- D141 pad 1: /PWR_LEDS -> +4V
- D142 pad 1: /PWR_LEDS -> +4V
- D143 pad 1: /PWR_LEDS -> +4V
- D144 pad 1: /PWR_LEDS -> +4V
- D145 pad 1: /PWR_LEDS -> +4V
- D146 pad 1: /PWR_LEDS -> +4V
- D147 pad 1: /PWR_LEDS -> +4V
- D148 pad 1: /PWR_LEDS -> +4V
- D149 pad 1: /PWR_LEDS -> +4V
- D15 pad 1: /PWR_LEDS -> +4V
- D150 pad 1: /PWR_LEDS -> +4V
- D151 pad 1: /PWR_LEDS -> +4V
- D152 pad 1: /PWR_LEDS -> +4V
- D153 pad 1: /PWR_LEDS -> +4V
- D154 pad 1: /PWR_LEDS -> +4V
- D155 pad 1: /PWR_LEDS -> +4V
- D156 pad 1: /PWR_LEDS -> +4V
- D157 pad 1: /PWR_LEDS -> +4V
- D158 pad 1: /PWR_LEDS -> +4V
- D159 pad 1: /PWR_LEDS -> +4V
- D16 pad 1: /PWR_LEDS -> +4V
- D160 pad 1: /PWR_LEDS -> +4V
- D161 pad 1: /PWR_LEDS -> +4V
- D162 pad 1: /PWR_LEDS -> +4V
- D163 pad 1: /PWR_LEDS -> +4V
- D164 pad 1: /PWR_LEDS -> +4V
- D165 pad 1: /PWR_LEDS -> +4V
- D166 pad 1: /PWR_LEDS -> +4V
- D167 pad 1: /PWR_LEDS -> +4V
- D168 pad 1: /PWR_LEDS -> +4V
- D169 pad 1: /PWR_LEDS -> +4V
- D17 pad 1: /PWR_LEDS -> +4V
- D170 pad 1: /PWR_LEDS -> +4V
- D171 pad 1: /PWR_LEDS -> +4V
- D172 pad 1: /PWR_LEDS -> +4V
- D173 pad 1: /PWR_LEDS -> +4V
- D174 pad 1: /PWR_LEDS -> +4V
- D175 pad 1: /PWR_LEDS -> +4V
- D176 pad 1: /PWR_LEDS -> +4V
- D177 pad 1: /PWR_LEDS -> +4V
- D178 pad 1: /PWR_LEDS -> +4V
- D179 pad 1: /PWR_LEDS -> +4V
- D18 pad 1: /PWR_LEDS -> +4V
- D180 pad 1: /PWR_LEDS -> +4V
- D181 pad 1: /PWR_LEDS -> +4V
- D182 pad 1: /PWR_LEDS -> +4V
- D183 pad 1: /PWR_LEDS -> +4V
- D184 pad 1: /PWR_LEDS -> +4V
- D185 pad 1: /PWR_LEDS -> +4V
- D186 pad 1: /PWR_LEDS -> +4V
- D187 pad 1: /PWR_LEDS -> +4V
- D188 pad 1: /PWR_LEDS -> +4V
- D189 pad 1: /PWR_LEDS -> +4V
- D19 pad 1: /PWR_LEDS -> +4V
- D190 pad 1: /PWR_LEDS -> +4V
- D191 pad 1: /PWR_LEDS -> +4V
- D192 pad 1: /PWR_LEDS -> +4V
- D193 pad 1: /PWR_LEDS -> +4V
- D194 pad 1: /PWR_LEDS -> +4V
- D195 pad 1: /PWR_LEDS -> +4V
- D196 pad 1: /PWR_LEDS -> +4V
- D197 pad 1: /PWR_LEDS -> +4V
- D198 pad 1: /PWR_LEDS -> +4V
- D199 pad 1: /PWR_LEDS -> +4V
- D20 pad 1: /PWR_LEDS -> +4V
- D200 pad 1: /PWR_LEDS -> +4V
- D201 pad 1: /PWR_LEDS -> +4V
- D202 pad 1: /PWR_LEDS -> +4V
- D203 pad 1: /PWR_LEDS -> +4V
- D204 pad 1: /PWR_LEDS -> +4V
- D205 pad 1: /PWR_LEDS -> +4V
- D206 pad 1: /PWR_LEDS -> +4V
- D207 pad 1: /PWR_LEDS -> +4V
- D208 pad 1: /PWR_LEDS -> +4V
- D209 pad 1: /PWR_LEDS -> +4V
- D21 pad 1: /PWR_LEDS -> +4V
- D210 pad 1: /PWR_LEDS -> +4V
- D211 pad 1: /PWR_LEDS -> +4V
- D212 pad 1: /PWR_LEDS -> +4V
- D213 pad 1: /PWR_LEDS -> +4V
- D214 pad 1: /PWR_LEDS -> +4V
- D215 pad 1: /PWR_LEDS -> +4V
- D216 pad 1: /PWR_LEDS -> +4V
- D217 pad 1: /PWR_LEDS -> +4V
- D218 pad 1: /PWR_LEDS -> +4V
- D219 pad 1: /PWR_LEDS -> +4V
- D22 pad 1: /PWR_LEDS -> +4V
- D220 pad 1: /PWR_LEDS -> +4V
- D221 pad 1: /PWR_LEDS -> +4V
- D222 pad 1: /PWR_LEDS -> +4V
- D223 pad 1: /PWR_LEDS -> +4V
- D224 pad 1: /PWR_LEDS -> +4V
- D225 pad 1: /PWR_LEDS -> +4V
- D226 pad 1: /PWR_LEDS -> +4V
- D227 pad 1: /PWR_LEDS -> +4V
- D228 pad 1: /PWR_LEDS -> +4V
- D229 pad 1: /PWR_LEDS -> +4V
- D23 pad 1: /PWR_LEDS -> +4V
- D230 pad 1: /PWR_LEDS -> +4V
- D231 pad 1: /PWR_LEDS -> +4V
- D232 pad 1: /PWR_LEDS -> +4V
- D233 pad 1: /PWR_LEDS -> +4V
- D234 pad 1: /PWR_LEDS -> +4V
- D235 pad 1: /PWR_LEDS -> +4V
- D236 pad 1: /PWR_LEDS -> +4V
- D237 pad 1: /PWR_LEDS -> +4V
- D238 pad 1: /PWR_LEDS -> +4V
- D239 pad 1: /PWR_LEDS -> +4V
- D24 pad 1: /PWR_LEDS -> +4V
- D240 pad 1: /PWR_LEDS -> +4V
- D241 pad 1: /PWR_LEDS -> +4V
- D242 pad 1: /PWR_LEDS -> +4V
- D243 pad 1: /PWR_LEDS -> +4V
- D244 pad 1: /PWR_LEDS -> +4V
- D245 pad 1: /PWR_LEDS -> +4V
- D246 pad 1: /PWR_LEDS -> +4V
- D247 pad 1: /PWR_LEDS -> +4V
- D248 pad 1: /PWR_LEDS -> +4V
- D249 pad 1: /PWR_LEDS -> +4V
- D25 pad 1: /PWR_LEDS -> +4V
- D250 pad 1: /PWR_LEDS -> +4V
- D251 pad 1: /PWR_LEDS -> +4V
- D252 pad 1: /PWR_LEDS -> +4V
- D253 pad 1: /PWR_LEDS -> +4V
- D254 pad 1: /PWR_LEDS -> +4V
- D255 pad 1: /PWR_LEDS -> +4V
- D256 pad 1: /PWR_LEDS -> +4V
- D257 pad 1: /PWR_LEDS -> +4V
- D258 pad 1: /PWR_LEDS -> +4V
- D259 pad 1: /PWR_LEDS -> +4V
- D26 pad 1: /PWR_LEDS -> +4V
- D260 pad 1: /PWR_LEDS -> +4V
- D27 pad 1: /PWR_LEDS -> +4V
- D28 pad 1: /PWR_LEDS -> +4V
- D29 pad 1: /PWR_LEDS -> +4V
- D3 pad 2: +4V -> /LIPO_PRE_MOSFET
- D30 pad 1: /PWR_LEDS -> +4V
- D31 pad 1: /PWR_LEDS -> +4V
- D32 pad 1: /PWR_LEDS -> +4V
- D33 pad 1: /PWR_LEDS -> +4V
- D34 pad 1: /PWR_LEDS -> +4V
- D35 pad 1: /PWR_LEDS -> +4V
- D36 pad 1: /PWR_LEDS -> +4V
- D37 pad 1: /PWR_LEDS -> +4V
- D38 pad 1: /PWR_LEDS -> +4V
- D39 pad 1: /PWR_LEDS -> +4V
- D4 pad 2: +4V -> /LIPO_PRE_MOSFET
- D40 pad 1: /PWR_LEDS -> +4V
- D41 pad 1: /PWR_LEDS -> +4V
- D42 pad 1: /PWR_LEDS -> +4V
- D43 pad 1: /PWR_LEDS -> +4V
- D44 pad 1: /PWR_LEDS -> +4V
- D45 pad 1: /PWR_LEDS -> +4V
- D46 pad 1: /PWR_LEDS -> +4V
- D47 pad 1: /PWR_LEDS -> +4V
- D48 pad 1: /PWR_LEDS -> +4V
- D49 pad 1: /PWR_LEDS -> +4V
- D5 pad 1: /PWR_LEDS -> +4V
- D50 pad 1: /PWR_LEDS -> +4V
- D51 pad 1: /PWR_LEDS -> +4V
- D52 pad 1: /PWR_LEDS -> +4V
- D53 pad 1: /PWR_LEDS -> +4V
- D54 pad 1: /PWR_LEDS -> +4V
- D55 pad 1: /PWR_LEDS -> +4V
- D56 pad 1: /PWR_LEDS -> +4V
- D57 pad 1: /PWR_LEDS -> +4V
- D58 pad 1: /PWR_LEDS -> +4V
- D59 pad 1: /PWR_LEDS -> +4V
- D6 pad 1: /PWR_LEDS -> +4V
- D60 pad 1: /PWR_LEDS -> +4V
- D61 pad 1: /PWR_LEDS -> +4V
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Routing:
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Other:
- board size 115.5 x 44.5 mm -> 112.5 x 42 mm

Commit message: routing and shape definiton in progress
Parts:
- added TP1: WS_IN, TestPoint:TestPoint_Pad_D1.5mm, B.Cu at (77.3, 84.0)
- added TP2: WS_IN, TestPoint:TestPoint_Pad_D1.5mm, B.Cu at (77.3, 87.5)
- added TP3: WS_IN, TestPoint:TestPoint_Pad_D1.5mm, B.Cu at (77.3, 91.1)
- moved SW3 39.3 mm to (174.8, 103.7), turned to 0 degrees
- moved C6 34.5 mm to (89.8, 100.8), turned to 0 degrees
- moved C9 29.8 mm to (93.0, 103.5), turned to 90 degrees
- moved R1 26.9 mm to (124.5, 105.8), turned to 180 degrees
- moved R17 25.4 mm to (113.5, 102.5), turned to -90 degrees
- moved C7 22.1 mm to (117.8, 101.0), turned to 180 degrees
- moved R21 21.4 mm to (108.8, 105.0)
- moved R20 21.1 mm to (107.5, 103.0), turned to 90 degrees
- moved R7 20.9 mm to (83.5, 103.8)
- moved R16 20.4 mm to (120.2, 102.5)
- moved R8 18.8 mm to (88.5, 102.0)
- moved C8 18.7 mm to (119.8, 105.2), turned to -90 degrees
- moved C180 18.7 mm to (112.0, 105.0)
- moved R19 18.3 mm to (110.5, 105.0)
- moved R18 12.5 mm to (113.2, 104.0), turned to 0 degrees
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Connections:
- D5 pad 4: /WS_2columns/DIN -> /WS_OUT
- U3 pad 31: unconnected-(U3-Pad31) -> /WS_OUT
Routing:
- net GND: track 35.0 -> 565.7 mm, vias 0 -> 7
- net +4V: track 34.6 -> 562.1 mm
- net VBUS: track 0.00 -> 54.7 mm
- net /ESP_EN: track 0.00 -> 42.1 mm
- net /PROG_RX: track 0.00 -> 39.8 mm
- net /PROG_TX: track 0.00 -> 37.0 mm
- net /ESP_BOOT: track 0.00 -> 18.7 mm, vias 0 -> 1
- net Net-(J1-PadA5): track 0.00 -> 10.5 mm
- net Net-(J1-PadB5): track 0.00 -> 7.49 mm
- net /WS_2columns2/DOUT: track 0.00 -> 5.55 mm, vias 0 -> 2
- net /WS_2columns6/DIN: track 0.00 -> 5.54 mm, vias 0 -> 2
- net /WS_2columns14/DIN: track 0.00 -> 5.54 mm, vias 0 -> 2
- net /WS_2columns11/DIN: track 0.00 -> 5.54 mm, vias 0 -> 2
- net /WS_2columns1/DOUT: track 0.00 -> 5.54 mm, vias 0 -> 2
- net /WS_2columns10/DOUT: track 0.00 -> 5.41 mm, vias 0 -> 2
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- added copper zone on B.Cu, net GND
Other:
- board size 112.5 x 42 mm -> 112.5 x 41.5 mm
- board text added: "CHG"
- board text added: "PWR"
- board text added: "USB"

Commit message: add changes for review
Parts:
- added JP1: TSNS_DIS, Jumper:SolderJumper-2_P1.3mm_Open_TrianglePad1.0x1.5mm, F.Cu at (144.1, 102.5)
- added TH1: NTC_10K, TestPoint:TestPoint_2Pads_Pitch2.54mm_Drill0.8mm, F.Cu at (147.2, 102.5)
- R16, R17: footprint Resistor_SMD:R_0201_0603Metric -> Resistor_SMD:R_0603_1608Metric_Pad0.98x0.95mm_HandSolder
- moved R18 26.0 mm to (139.3, 104.5), turned to 180 degrees
- moved TP3 16.8 mm to (78.2, 74.3)
- moved TP2 10.9 mm to (78.2, 76.7)
- moved TP1 4.77 mm to (78.1, 79.3)
- moved R16 1.68 mm to (121.6, 103.5)
- moved Q4 0.75 mm to (125.0, 103.5)
- moved R17 0.40 mm to (113.5, 102.9), turned to 90 degrees
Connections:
- U3 pad 14: /I2C_RST -> unconnected-(U3-Pad14)
- U3 pad 16: /IN_BUFF_ENA -> unconnected-(U3-Pad16)
- U3 pad 24: /LED_STATUS -> unconnected-(U3-Pad24)
- U3 pad 26: /SCL -> unconnected-(U3-Pad26)
- U3 pad 29: /SDA -> unconnected-(U3-Pad29)
- U3 pad 31: /WS_OUT -> unconnected-(U3-Pad31)
- U3 pad 36: unconnected-(U3-Pad36) -> /WS_OUT
- U5 pad 1: Net-(R18-Pad2) -> Net-(U5-Pad1)
- U5 pad 5: +4V -> /LIPO_PRE_MOSFET
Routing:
- net /ESP_BOOT: track 18.7 -> 150.1 mm, vias 1 -> 4
- net unconnected-(SW1-Pad2): track 0.00 -> 80.2 mm, vias 0 -> 2
- net Net-(Q4-Pad1): track 0.00 -> 52.6 mm, vias 0 -> 2
- net Net-(U5-Pad1): track 0.00 -> 39.0 mm, vias 0 -> 1
- net GND: track 565.7 -> 582.2 mm, vias 7 -> 10
- net /WS_OUT: track 0.00 -> 10.4 mm, vias 0 -> 1
- net Net-(R18-Pad2): track 0.00 -> 5.82 mm
- net +4V: track 562.1 -> 567.2 mm, vias 0 -> 1
- net /PROG_RX: track 39.8 -> 36.6 mm
- net Net-(R17-Pad2): track 0.00 -> 2.88 mm
- net /PROG_TX: track 37.0 -> 34.5 mm
- net Net-(J1-PadB5): track 7.49 -> 6.82 mm
- net /WS_2columns/DOUT: track 5.92 -> 5.35 mm
